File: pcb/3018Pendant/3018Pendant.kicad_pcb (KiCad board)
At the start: 2 copper layers, 70.5 x 39.4 mm, 10 parts, among them J1 Conn_02x04_Odd_Even, J2 SW 1, J3 GND, J4 Vcc, J5 Encoder 1, J6 SW 2, J7 SW XYZ, U1 Arduino_Pro_Mini

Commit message: update readme
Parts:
- J2, J6: footprint Connector_PinHeader_2.54mm:PinHeader_1x01_P2.54mm_Horizontal -> Connector_PinHeader_2.54mm:PinHeader_1x01_P2.54mm_Vertical
- J5: footprint Connector_PinHeader_2.54mm:PinHeader_1x02_P2.54mm_Horizontal -> Connector_PinHeader_2.54mm:PinHeader_1x02_P2.54mm_Vertical
- J7: footprint Connector_PinHeader_2.54mm:PinHeader_1x03_P2.54mm_Horizontal -> Connector_PinHeader_2.54mm:PinHeader_1x03_P2.54mm_Vertical

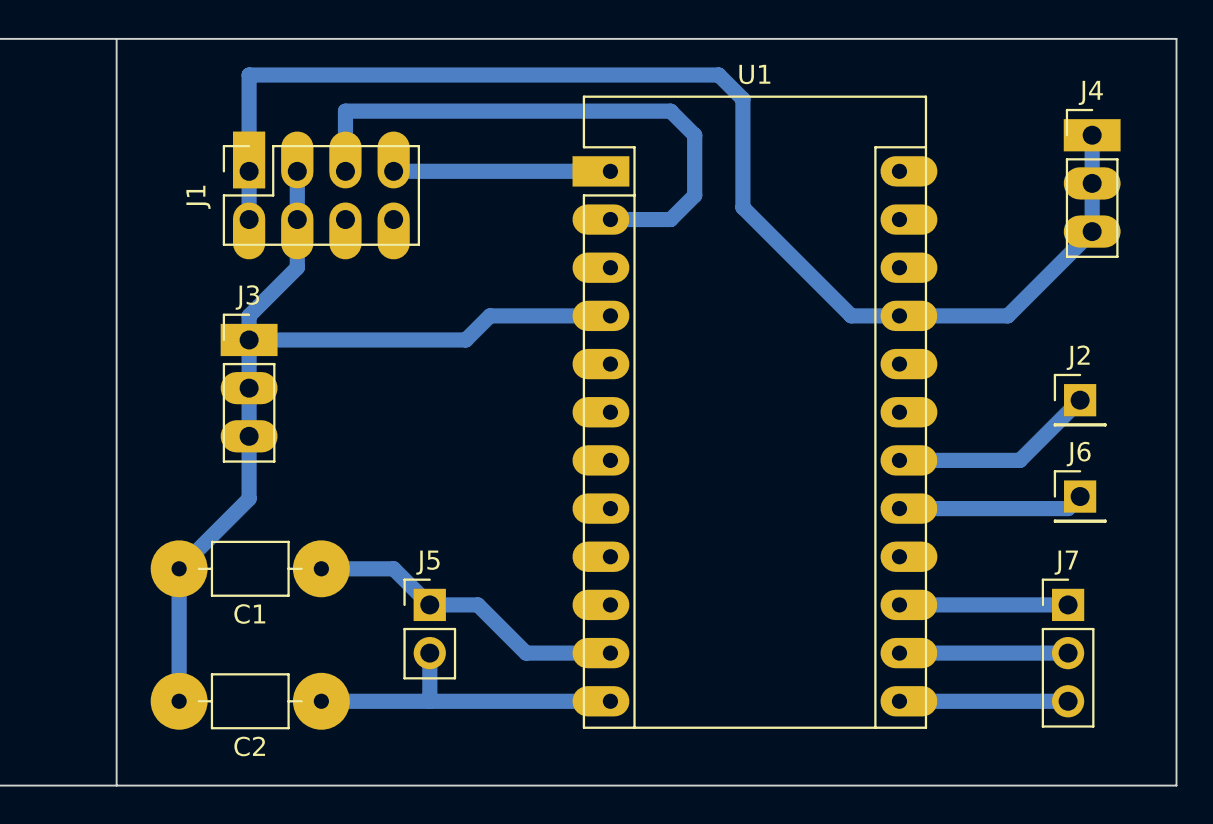
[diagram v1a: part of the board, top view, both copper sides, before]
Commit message: Update schematic & PCB to include reset button
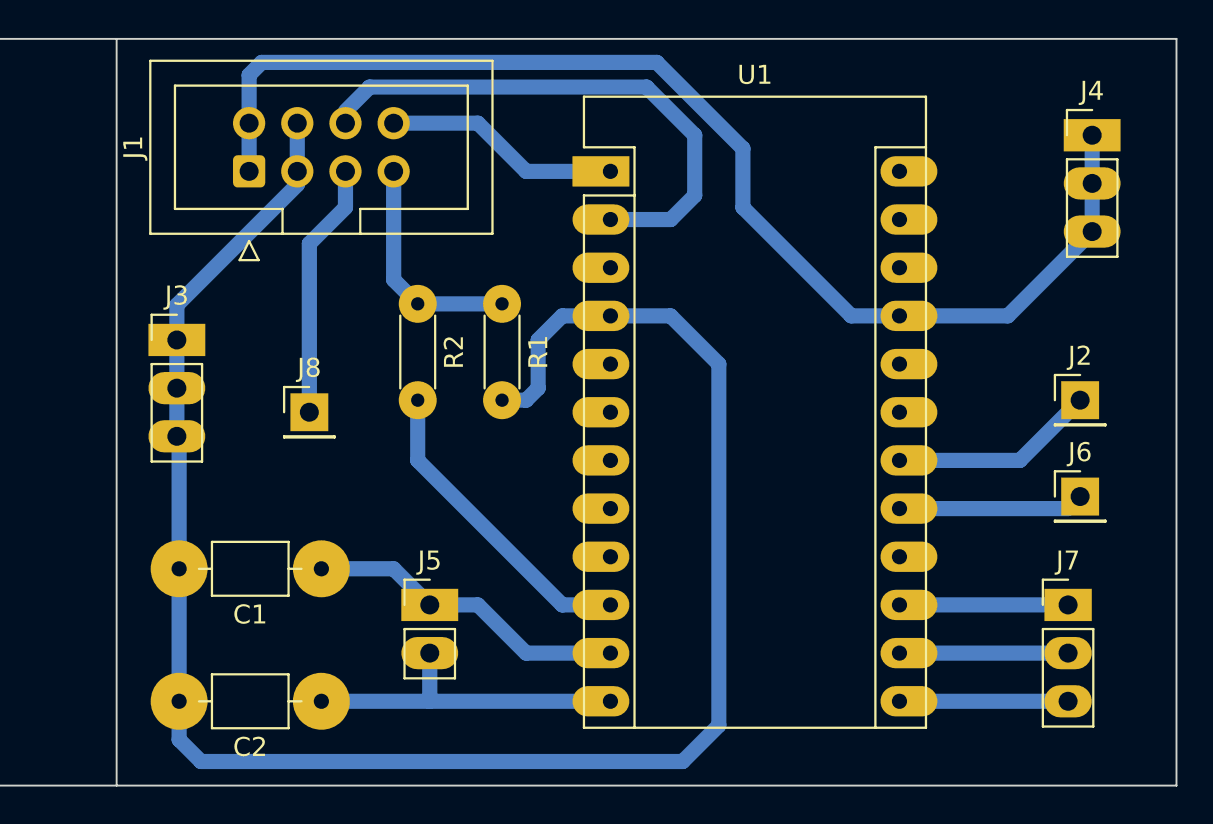
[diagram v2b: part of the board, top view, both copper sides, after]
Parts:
- added J8: SW RESET, Connector_PinHeader_2.54mm:PinHeader_1x01_P2.54mm_Vertical, F.Cu at (74.9, -21.0)
- added R1: 1K, Resistor_THT:R_Axial_DIN0204_L3.6mm_D1.6mm_P5.08mm_Horizontal, F.Cu at (85.1, -26.7)
- added R2: 1K, Resistor_THT:R_Axial_DIN0204_L3.6mm_D1.6mm_P5.08mm_Horizontal, F.Cu at (80.6, -26.7)
- J1: footprint Connector_PinSocket_2.54mm:PinSocket_2x04_P2.54mm_Vertical -> Connector_IDC:IDC-Header_2x04_P2.54mm_Vertical
- moved J3 3.81 mm to (67.9, -24.8)
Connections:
- U1 pad 1: Net-(J1-Pad7) -> Net-(J1-Pad8)
- U1 pad 2: Net-(J1-Pad5) -> Net-(J1-Pad6)
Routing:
- net GND: track 50.1 -> 99.8 mm
- net Net-(J1-Pad6): track 0.00 -> 28.1 mm
- net Net-(J1-Pad5): track 30.3 -> 13.5 mm
- net Net-(R2-Pad2): track 0.00 -> 16.5 mm
- net Net-(J1-Pad8): track 0.00 -> 12.5 mm
- net Vcc: track 67.6 -> 64.1 mm
- net Net-(J1-Pad7): track 11.4 -> 12.0 mm

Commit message: Add LED
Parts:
- added D1: LED, LED_THT:LED_D3.0mm_Clear, F.Cu at (169.5, 87.0)
- added R3: 1K, Resistor_THT:R_Axial_DIN0204_L3.6mm_D1.6mm_P5.08mm_Horizontal, F.Cu at (169.5, 80.0)
- moved J6 116.2 mm to (164.5, 88.9)
- moved C1 116.2 mm to (124.5, 92.7)
- moved C2 116.2 mm to (124.5, 99.7)
- moved J1 116.2 mm to (120.7, 71.8)
- moved J2 116.2 mm to (164.5, 83.8)
- moved J3 116.2 mm to (116.8, 80.6)
- moved J4 116.2 mm to (165.1, 69.8)
- moved J5 116.2 mm to (130.2, 94.6)
- moved J7 116.2 mm to (163.8, 94.6)
- moved J8 116.2 mm to (123.8, 84.5)
- moved R1 116.2 mm to (134.0, 78.7)
- moved R2 116.2 mm to (129.5, 78.7)
- moved U1 116.2 mm to (139.7, 71.8)
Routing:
- net GND: track 99.8 -> 142.0 mm
- net Net-(R3-Pad2): track 0.00 -> 10.3 mm
- net Net-(D1-Pad2): track 0.00 -> 4.44 mm
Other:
- board size 70.5 x 39.4 mm -> 78.7 x 39.4 mm

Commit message: final version
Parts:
- moved J1 77.3 mm to (50.8, 38.7)
- moved J2 77.3 mm to (94.6, 50.8)
- moved J5 77.3 mm to (60.3, 61.6)
- moved J6 77.3 mm to (94.6, 55.9)
- moved J7 77.3 mm to (94.0, 61.6)
- moved R1 77.3 mm to (64.1, 45.7)
- moved C1 77.3 mm to (54.6, 59.7)
- moved C2 77.3 mm to (54.6, 66.7)
- moved D1 77.3 mm to (99.7, 54.0)
- moved J3 77.3 mm to (47.0, 47.6)
- moved J4 77.3 mm to (95.2, 36.8)
- moved J8 77.3 mm to (54.0, 51.4)
- moved R2 77.3 mm to (59.7, 45.7)
- moved R3 77.3 mm to (99.7, 47.0)
- moved U1 77.3 mm to (69.8, 38.7)
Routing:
- net Vcc: track 64.1 -> 68.9 mm
